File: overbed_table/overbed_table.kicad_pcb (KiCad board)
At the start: 2 copper layers, 51 x 87.5 mm, 78 parts, among them CN10 DLL-5569-2AW, CN2 KF2EDGRC-5.08-4P, CN3 KF2EDGRC-5.08-4P, CN8 DLL-5569-2AW, CN9 DLL-5569-2AW, Q1 BSS138, Q2 BSS138, Q3 BSS138, Q4 AON7524, Q5 AON7524, Q6 AON7524, SW1 KH-6X6X6H-STM, SW2 KH-6X6X6H-STM, U1 AP2112K-3.3TRG1, U10 TPS562201DDCR, U11 TPS562201DDCR, U15 SP3485EN, U2 ESP32-C3-WROOM-02, U3 WAFER-XH254WZ-2A, U4 BSMD2920-500-24V, U5 BSMD2920-500-24V, U6 BSMD2920-500-24V, U7 KF7620-7.62-2P, X1 AFA01-S05FCA-00

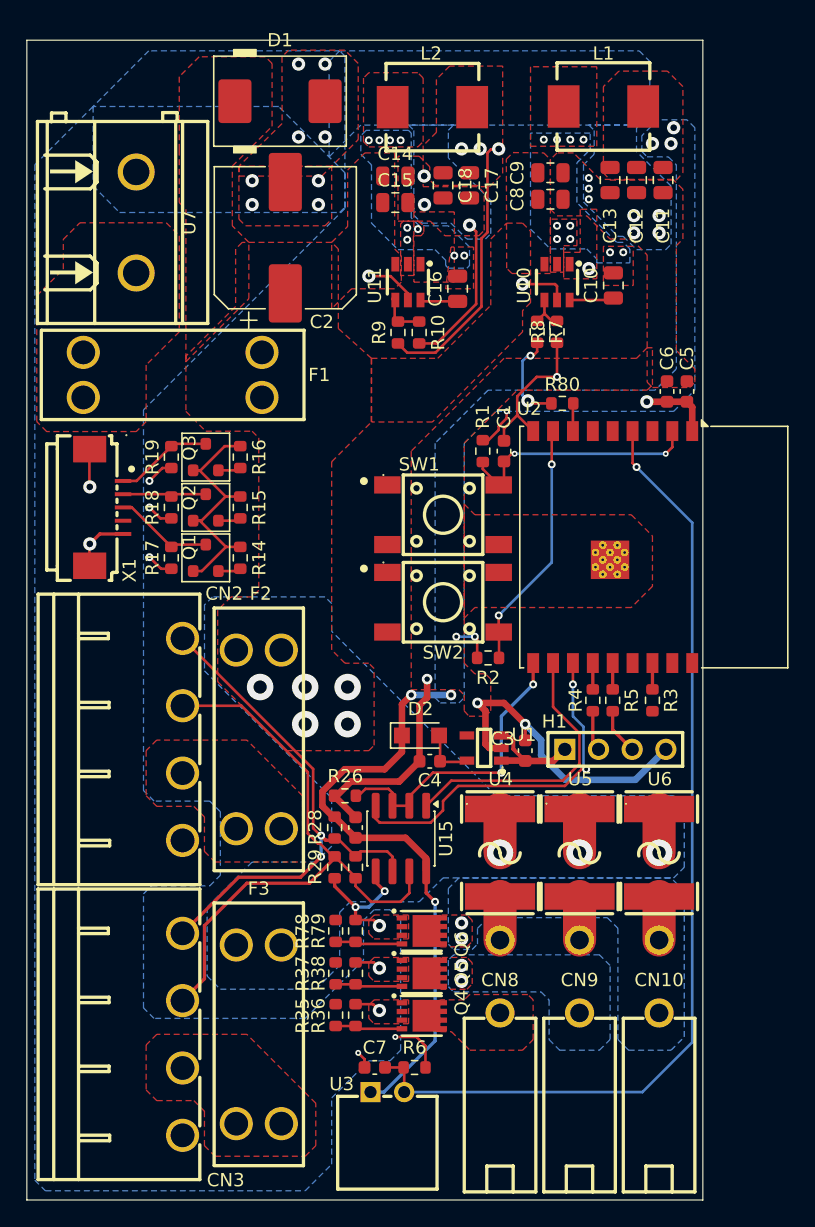
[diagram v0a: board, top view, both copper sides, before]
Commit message: update: 更新ESP32 PCB
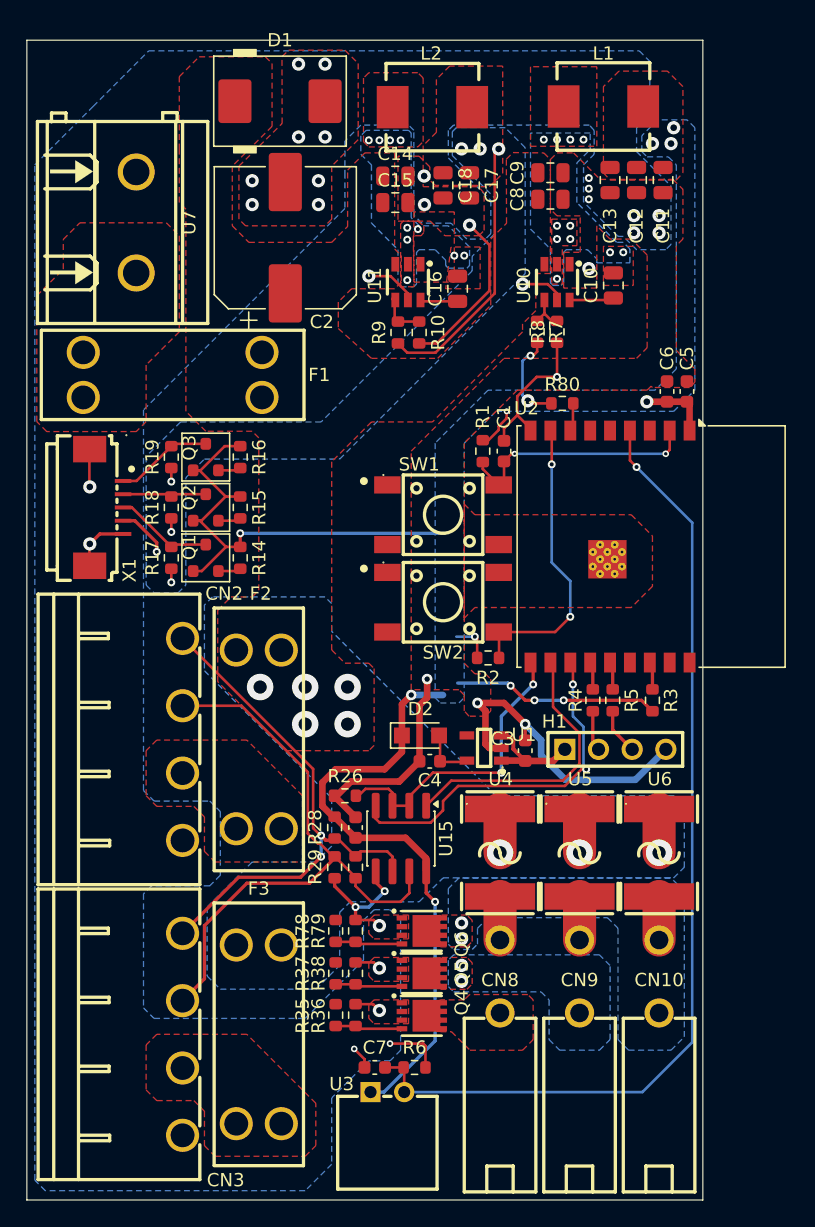
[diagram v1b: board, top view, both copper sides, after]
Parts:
- moved U2 0.20 mm to (69.0, 63.2)
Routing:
- net /+3V3: track 84.2 -> 115.9 mm, vias 12 -> 14
- net /ESP32_BOOT: track 18.8 -> 22.5 mm
- net /GND: track 91.0 -> 92.4 mm
- net /+5V: track 26.8 -> 27.6 mm, vias 6 -> 7
- net Net-(U11-SW): vias 9 -> 10
- net Net-(U10-SW): vias 10 -> 11
- added copper zone on B.Cu, net /+5V

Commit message: update: 更新ESP32 PCB V1.0.0
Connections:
- U2 pad 15: /3V3_5V_转换器/3V3_SIG2 -> /LED3_PWM
- U2 pad 17: /3V3_5V_转换器/3V3_SIG1 -> /LED2_PWM
- U2 pad 18: /3V3_5V_转换器/3V3_SIG0 -> /LED1_PWM
- U2 pad 3: /LED1_PWM -> /3V3_5V_转换器/3V3_SIG0
- U2 pad 5: /LED2_PWM -> /3V3_5V_转换器/3V3_SIG1
- U2 pad 6: /LED3_PWM -> /3V3_5V_转换器/3V3_SIG2
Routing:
- net /LED1_PWM: track 0.00 -> 63.0 mm, vias 0 -> 4
- net /LED2_PWM: track 0.00 -> 54.6 mm, vias 0 -> 4
- net /LED3_PWM: track 0.00 -> 46.7 mm, vias 0 -> 4
- net /3V3_5V_转换器/3V3_SIG0: track 1.72 -> 40.3 mm, vias 0 -> 2
- net /3V3_5V_转换器/3V3_SIG1: track 1.72 -> 33.6 mm, vias 0 -> 2
- net /3V3_5V_转换器/3V3_SIG2: track 1.72 -> 32.4 mm, vias 0 -> 2
- net /GND: track 92.4 -> 109.3 mm
- net /ESP32_BOOT: track 22.5 -> 21.3 mm
- net /RS485_ESP32/RS485_N: track 46.6 -> 45.6 mm

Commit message: update: 更新侧板PCB
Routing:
- net /GND: track 109.3 -> 105.7 mm, vias 32 -> 31
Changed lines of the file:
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@@
+	)
+	(segment
+		(start 65 47.825)
+		(end 65 49.6)
+		(width 0.2)
+		(layer "F.Cu")
+		(net "/GND")
 	)
 	(segment
@@
 	)
 	(segment
-		(start 62 51.868629)
-		(end 63.468629 50.4)
-		(width 0.2)
-		(layer "F.Cu")
-		(net "/GND")
-	)
-	(segment
 		(start 59.9 40.45)
 		(end 58.4 38.95)
@@
 	)
 	(segment
-		(start 63.468629 50.4)
-		(end 65 50.4)
-		(width 0.2)
-		(layer "F.Cu")
-		(net "/GND")
-	)
-	(segment
 		(start 29.72 65.35)
 		(end 29.72 63.03)
@@
 	)
 	(segment
-		(start 65 47.825)
-		(end 65 50.4)
-		(width 0.2)
-		(layer "F.Cu")
-		(net "/GND")
-	)
-	(segment
 		(start 29.72 58.67)
 		(end 29.75 58.7)
@@
 	)
 	(segment
+		(start 62 53.29)
+		(end 62 51)
+		(width 0.2)
+		(layer "F.Cu")
+		(net "/GND")
+	)
+	(segment
 		(start 54.9 100.7)
 		(end 55.075 100.875)
@@
 		(start 29.72 62.97)
 		(end 29.75 63)
-		(width 0.2)
-		(layer "F.Cu")
-		(net "/GND")
-	)
-	(segment
-		(start 62 53.29)
-		(end 62 51.868629)
 		(width 0.2)
 		(layer "F.Cu")
@@
 	)
 	(via
-		(at 65 50.4)
-		(size 0.6)
-		(drill 0.3)
-		(layers "F.Cu" "B.Cu")
-		(net "/GND")
-	)
-	(via
 		(at 29.75 58.7)
 		(size 1)
@@
 	)
 	(segment
-		(start 43.4 88.425)
-		(end 42.6 87.625)
+		(start 42.5 82.1)
+		(end 45.4 79.2)
+		(width 0.2)
+		(layer "B.Cu")
+		(net "/LED1_PWM")
+	)
+	(segment
+		(start 42.5 87.525)
+		(end 42.5 82.1)
 		(width 0.2)
 		(layer "B.Cu")
@@
 	)
 	(segment
-		(start 42.6 87.625)
-		(end 42.6 82)
+		(start 43.4 88.425)
+		(end 42.5 87.525)
 		(width 0.2)
 		(layer "B.Cu")
@@
 	)
 	(segment
-		(start 42.6 82)
-		(end 45.4 79.2)
-		(width 0.2)
-		(layer "B.Cu")
-		(net "/LED1_PWM")
-	)
-	(segment
 		(start 65.95 44.6)
 		(end 69.1 44.6)
@@
 	)
 	(segment
+		(start 41.1 64.875)
+		(end 42.060856 63.914144)
+		(width 0.2)
+		(layer "F.Cu")
+		(net "/3V3_5V_转换器/3V3_SIG0")
+	)
+	(segment
+		(start 72 57.048529)
+		(end 72 54.45)
+		(width 0.2)
+		(layer "F.Cu")
+		(net "/3V3_5V_转换器/3V3_SIG0")
+	)
+	(segment
+		(start 57 60.2)
+		(end 57.4 60.6)
+		(width 0.2)
+		(layer "F.Cu")
+		(net "/3V3_5V_转换器/3V3_SIG0")
+	)
+	(segment
+		(start 57.4 60.6)
+		(end 68.448529 60.6)
+		(width 0.2)
+		(layer "F.Cu")
+		(net "/3V3_5V_转换器/3V3_SIG0")
+	)
+	(segment
+		(start 42.060856 63.914144)
+		(end 42.060856 61.415053)
+		(width 0.2)
+		(layer "F.Cu")
+		(net "/3V3_5V_转换器/3V3_SIG0")
+	)
+	(segment
+		(start 39.45 65.05)
+		(end 40.925 65.05)
+		(width 0.2)
+		(layer "F.Cu")
+		(net "/3V3_5V_转换器/3V3_SIG0")
+	)
+	(segment
+		(start 40.925 65.05)
+		(end 41.1 64.875)
+		(width 0.2)
+		(layer "F.Cu")
+		(net "/3V3_5V_转换器/3V3_SIG0")
+	)
+	(segment
+		(start 68.448529 60.6)
+		(end 72 57.048529)
+		(width 0.2)
+		(layer "F.Cu")
+		(net "/3V3_5V_转换器/3V3_SIG0")
+	)
+	(via
+		(at 42.060856 61.415053)
+		(size 0.6)
+		(drill 0.3)
+		(layers "F.Cu" "B.Cu")
+		(net "/3V3_5V_转换器/3V3_SIG0")
+	)
+	(via
+		(at 57 60.2)
+		(size 0.6)
+		(drill 0.3)
+		(layers "F.Cu" "B.Cu")
+		(net "/3V3_5V_转换器/3V3_SIG0")
+	)
+	(segment
+		(start 43.275909 60.2)
+		(end 57 60.2)
+		(width 0.2)
+		(layer "B.Cu")
+		(net "/3V3_5V_转换器/3V3_SIG0")
+	)
+	(segment
+		(start 42.060856 61.415053)
+		(end 43.275909 60.2)
+		(width 0.2)
+		(layer "B.Cu")
+		(net "/3V3_5V_转换器/3V3_SIG0")
+	)
+	(segment
 		(start 53.47 104.3585)
 		(end 53.47 102.545)
@@
 	)
 	(segment
+		(start 57 58.2)
+		(end 58.4 59.6)
+		(width 0.2)
+		(layer "F.Cu")
+		(net "/3V3_5V_转换器/3V3_SIG2")
+	)
+	(segment
+		(start 41.1 57.275)
+		(end 41.1 57.7)
+		(width 0.2)
+		(layer "F.Cu")
+		(net "/3V3_5V_转换器/3V3_SIG2")
+	)
+	(segment
+		(start 41.1 57.7)
+		(end 41.6 58.2)
+		(width 0.2)
+		(layer "F.Cu")
+		(net "/3V3_5V_转换器/3V3_SIG2")
+	)
+	(segment
+		(start 39.45 57.45)
+		(end 40.925 57.45)
+		(width 0.2)
+		(layer "F.Cu")
+		(net "/3V3_5V_转换器/3V3_SIG2")
+	)
+	(segment
+		(start 64 59.6)
+		(end 67.5 56.1)
+		(width 0.2)
+		(layer "F.Cu")
+		(net "/3V3_5V_转换器/3V3_SIG2")
+	)
+	(segment
+		(start 58.4 59.6)
+		(end 64 59.6)
+		(width 0.2)
+		(layer "F.Cu")
+		(net "/3V3_5V_转换器/3V3_SIG2")
+	)
+	(segment
+		(start 67.5 56.1)
+		(end 67.5 54.45)
+		(width 0.2)
+		(layer "F.Cu")
+		(net "/3V3_5V_转换器/3V3_SIG2")
+	)
+	(segment
+		(start 40.925 57.45)
+		(end 41.1 57.275)
+		(width 0.2)
+		(layer "F.Cu")
+		(net "/3V3_5V_转换器/3V3_SIG2")
+	)
+	(via
+		(at 57 58.2)
+		(size 0.6)
+		(drill 0.3)
+		(layers "F.Cu" "B.Cu")
+		(net "/3V3_5V_转换器/3V3_SIG2")
+	)
+	(via
+		(at 41.6 58.2)
+		(size 0.6)
+		(drill 0.3)
+		(layers "F.Cu" "B.Cu")
+		(net "/3V3_5V_转换器/3V3_SIG2")
+	)
+	(segment
+		(start 41.6 58.2)
+		(end 57 58.2)
+		(width 0.2)
+		(layer "B.Cu")
+		(net "/3V3_5V_转换器/3V3_SIG2")
+	)
+	(segment
 		(start 66.2 54.49)
 		(end 66.2 52.425)
@@
 		(net "Net-(U2-IO19)")
 	)
-	(segment
-		(start 57 58.2)
-		(end 58.4 59.6)
-		(width 0.2)
-		(layer "F.Cu")
-		(net "/3V3_5V_转换器/3V3_SIG2")
-	)
-	(segment
-		(start 41.1 57.275)
-		(end 41.1 57.7)
-		(width 0.2)
-		(layer "F.Cu")
-		(net "/3V3_5V_转换器/3V3_SIG2")
-	)
-	(segment
-		(start 41.1 57.7)
-		(end 41.6 58.2)
-		(width 0.2)
-		(layer "F.Cu")
-		(net "/3V3_5V_转换器/3V3_SIG2")
-	)
-	(segment
-		(start 39.45 57.45)
-		(end 40.925 57.45)
-		(width 0.2)
-		(layer "F.Cu")
-		(net "/3V3_5V_转换器/3V3_SIG2")
-	)
-	(segment
-		(start 64 59.6)
-		(end 67.5 56.1)
-		(width 0.2)
-		(layer "F.Cu")
-		(net "/3V3_5V_转换器/3V3_SIG2")
-	)
-	(segment
-		(start 58.4 59.6)
-		(end 64 59.6)
-		(width 0.2)
-		(layer "F.Cu")
-		(net "/3V3_5V_转换器/3V3_SIG2")
-	)
-	(segment
-		(start 67.5 56.1)
-		(end 67.5 54.45)
-		(width 0.2)
-		(layer "F.Cu")
-		(net "/3V3_5V_转换器/3V3_SIG2")
-	)
-	(segment
-		(start 40.925 57.45)
-		(end 41.1 57.275)
-		(width 0.2)
-		(layer "F.Cu")
-		(net "/3V3_5V_转换器/3V3_SIG2")
-	)
-	(via
-		(at 57 58.2)
-		(size 0.6)
-		(drill 0.3)
-		(layers "F.Cu" "B.Cu")
-		(net "/3V3_5V_转换器/3V3_SIG2")
-	)
-	(via
-		(at 41.6 58.2)
-		(size 0.6)
-		(drill 0.3)
-		(layers "F.Cu" "B.Cu")
-		(net "/3V3_5V_转换器/3V3_SIG2")
-	)
-	(segment
-		(start 41.6 58.2)
-		(end 57 58.2)
-		(width 0.2)
-		(layer "B.Cu")
-		(net "/3V3_5V_转换器/3V3_SIG2")
-	)
-	(segment
-		(start 41.1 64.875)
-		(end 42.060856 63.914144)
-		(width 0.2)
-		(layer "F.Cu")
-		(net "/3V3_5V_转换器/3V3_SIG0")
-	)
-	(segment
-		(start 72 57.048529)
-		(end 72 54.45)
-		(width 0.2)
-		(layer "F.Cu")
-		(net "/3V3_5V_转换器/3V3_SIG0")
-	)
-	(segment
-		(start 57 60.2)
-		(end 57.4 60.6)
-		(width 0.2)
-		(layer "F.Cu")
-		(net "/3V3_5V_转换器/3V3_SIG0")
-	)
-	(segment
-		(start 57.4 60.6)
-		(end 68.448529 60.6)
-		(width 0.2)
-		(layer "F.Cu")
-		(net "/3V3_5V_转换器/3V3_SIG0")
-	)
-	(segment
-		(start 42.060856 63.914144)
-		(end 42.060856 61.415053)
-		(width 0.2)
-		(layer "F.Cu")
-		(net "/3V3_5V_转换器/3V3_SIG0")
-	)
-	(segment
-		(start 39.45 65.05)
-		(end 40.925 65.05)
-		(width 0.2)
-		(layer "F.Cu")
-		(net "/3V3_5V_转换器/3V3_SIG0")
-	)
-	(segment
-		(start 40.925 65.05)
-		(end 41.1 64.875)
-		(width 0.2)
-		(layer "F.Cu")
-		(net "/3V3_5V_转换器/3V3_SIG0")
-	)
-	(segment
-		(start 68.448529 60.6)
-		(end 72 57.048529)
-		(width 0.2)
-		(layer "F.Cu")
-		(net "/3V3_5V_转换器/3V3_SIG0")
-	)
-	(via
-		(at 42.060856 61.415053)
-		(size 0.6)
-		(drill 0.3)
-		(layers "F.Cu" "B.Cu")
-		(net "/3V3_5V_转换器/3V3_SIG0")
-	)
-	(via
-		(at 57 60.2)
-		(size 0.6)
-		(drill 0.3)
-		(layers "F.Cu" "B.Cu")
-		(net "/3V3_5V_转换器/3V3_SIG0")
-	)
-	(segment
-		(start 43.275909 60.2)
-		(end 57 60.2)
-		(width 0.2)
-		(layer "B.Cu")
-		(net "/3V3_5V_转换器/3V3_SIG0")
-	)
-	(segment
-		(start 42.060856 61.415053)
-		(end 43.275909 60.2)
-		(width 0.2)
-		(layer "B.Cu")
-		(net "/3V3_5V_转换器/3V3_SIG0")
-	)
-	(via
+	(via

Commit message: update: 更新主板电源指示灯
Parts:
- added D3: LED, LED_SMD:LED_0603_1608Metric, F.Cu at (50.6, 55.0)
- added D4: LED, LED_SMD:LED_0603_1608Metric, F.Cu at (73.8, 42.6)
- added D5: LED, LED_SMD:LED_0603_1608Metric, F.Cu at (62.0, 31.6)
- added R11: 10k, Resistor_SMD:R_0603_1608Metric, F.Cu at (52.2, 55.0)
- added R12: 1k, Resistor_SMD:R_0603_1608Metric, F.Cu at (73.8, 45.8)
- added R13: 1k, Resistor_SMD:R_0603_1608Metric, F.Cu at (73.8, 44.2)
- added R20: 4.7k, Resistor_SMD:R_0603_1608Metric, F.Cu at (62.0, 28.4)
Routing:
- net /GND: track 105.7 -> 109.8 mm, vias 31 -> 34
- net Net-(D3-K): track 0.00 -> 2.28 mm
- net /+5V: track 27.6 -> 29.3 mm
- net Net-(D4-K): track 0.00 -> 1.62 mm
- net Net-(R12-Pad2): track 0.00 -> 1.60 mm
- net Net-(D5-K): track 0.00 -> 1.59 mm
- net /+3V3: track 115.9 -> 117.4 mm, vias 14 -> 15
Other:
- board text added: "12V"
- board text added: "3V3"
- board text added: "5V"
- board text added: "Designed by 布谷鸟"

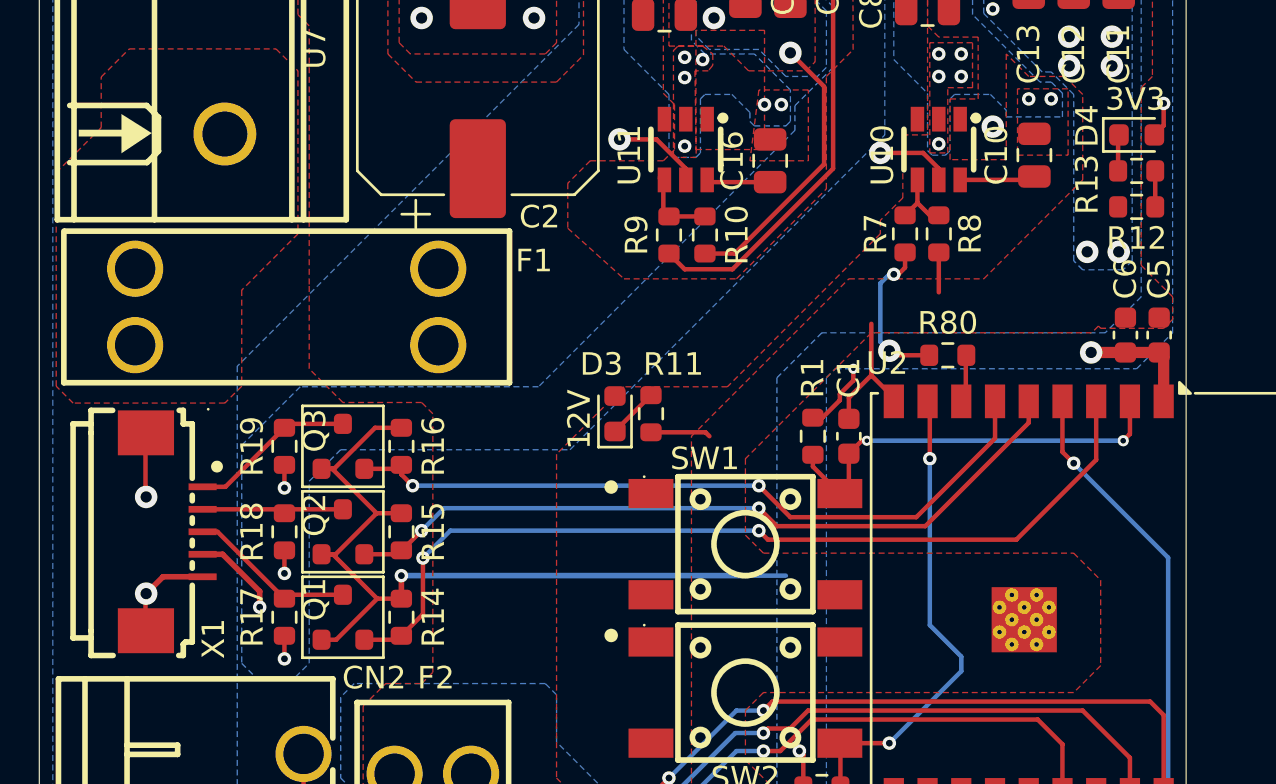
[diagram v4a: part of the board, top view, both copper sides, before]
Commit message: update: 添加主板测试点
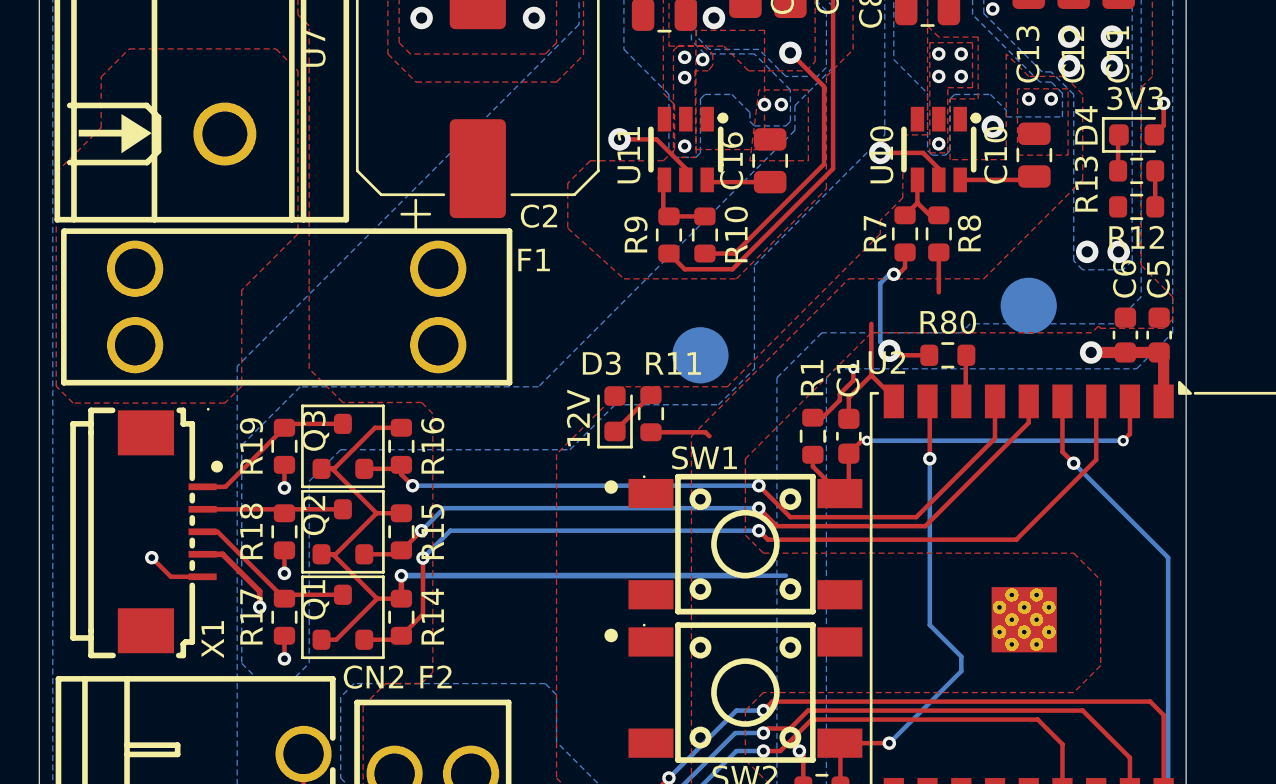
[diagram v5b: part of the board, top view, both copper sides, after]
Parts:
- added TP1: TestPoint, TestPoint:TestPoint_Pad_D2.5mm, B.Cu at (54.4, 52.4)
- added TP2: TestPoint, TestPoint:TestPoint_Pad_D2.5mm, B.Cu at (69.0, 50.2)
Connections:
- X1 pad 6: /GND -> unconnected-(X1-Pad6)
- X1 pad 7: /GND -> unconnected-(X1-Pad7)
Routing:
- net /GND: track 109.8 -> 105.0 mm, vias 34 -> 33
